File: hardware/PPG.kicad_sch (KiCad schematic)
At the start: 2 parts, among them IC2 MAX86141ENP+T, IC3 SFH_7074

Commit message: Added display block (barely) and freaked out about PPG stuff
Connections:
- net PPG_SCK: now reaches IC2.A2 (SCLK)
- net PPG_MISO: now reaches IC2.A3 (SDO)
- net PPG_MOSI: now reaches IC2.A4 (SDI)
- net PPG_CS: now reaches IC2.A5 (CSB)
- net GND: now reaches IC2.C2 (VDD_DIG)
- net GND: now also IC2.C3 (GND_DIG), IC2.C4 (GND_ANA), IC2.C5 (PD_GND), IC2.D3 (PGND)
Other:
- note added: "MAX86141 requires 1p8 power supply for both core and IO This would require a level translator to communicate with the STM32 Explore * AFE4404 * AFE4490 * OSRAM AS7058 What is my dynamic range requirement? What are my wavelengths? What does my optical stack look like? Can't choose an AFE until the above is settled ^^"

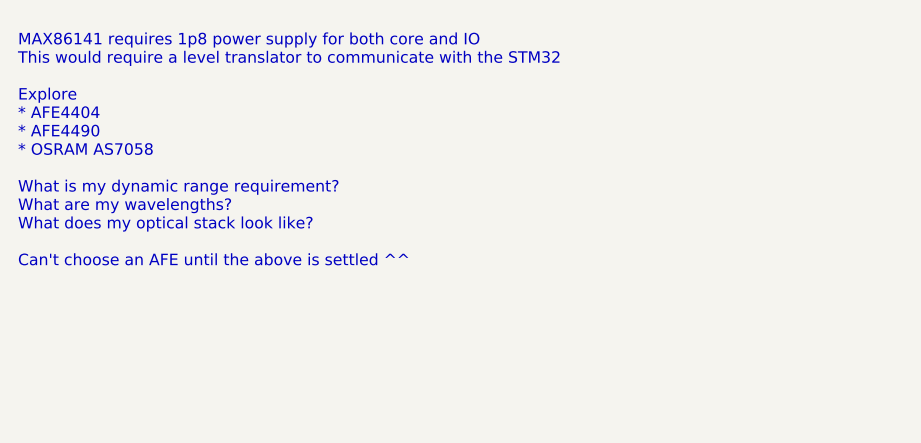
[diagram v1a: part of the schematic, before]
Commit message: Added bluetooth module schematic and environmental perception block"
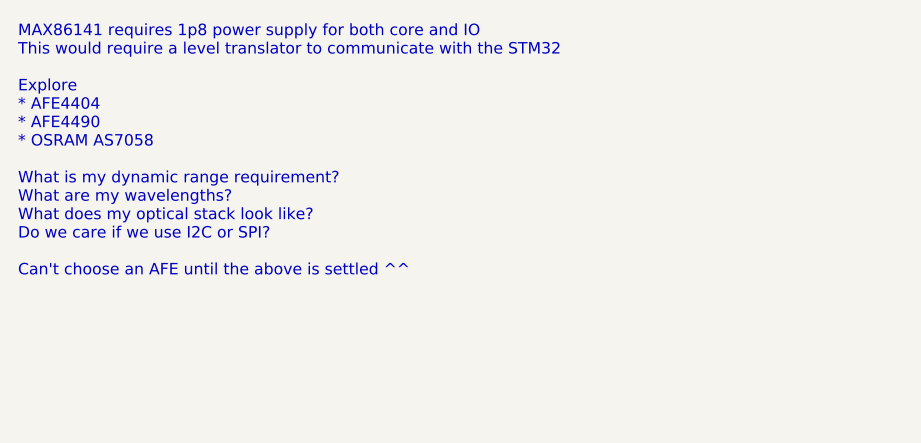
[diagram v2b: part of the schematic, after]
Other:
- note added: "MAX86141 requires 1p8 power supply for both core and IO This would require a level translator to communicate with the STM32 Explore * AFE4404 * AFE4490 * OSRAM AS7058 What is my dynamic range requirement? What are my wavelengths? What does my optical stack look like? Do we care if we use I2C or SPI? Can't choose an AFE until the above is settled ^^"
- note removed: "MAX86141 requires 1p8 power supply for both core and IO This would require a level translator to communicate with the STM32 Explore * AFE4404 * AFE4490 * OSRAM AS7058 What is my dynamic range requirement? What are my wavelengths? What does my optical stack look like? Can't choose an AFE until the above is settled ^^"
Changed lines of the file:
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@@
 	(generator_version "10.0")
 	(paper "A4")
-	(text "MAX86141 requires 1p8 power supply for both core and IO\nThis would require a level translator to communicate with the STM32\n\nExplore\n* AFE4404\n* AFE4490\n* OSRAM AS7058\n\nWhat is my dynamic range requirement?\nWhat are my wavelengths?\nWhat does my optical stack look like?\n\nCan't choose an AFE until the above is settled ^^"
+	(text "MAX86141 requires 1p8 power supply for both core and IO\nThis would require a level translator to communicate with the STM32\n\nExplore\n* AFE4404\n* AFE4490\n* OSRAM AS7058\n\nWhat is my dynamic range requirement?\nWhat are my wavelengths?\nWhat does my optical stack look like?\nDo we care if we use I2C or SPI?\n\nCan't choose an AFE until the above is settled ^^"
 		(exclude_from_sim no)
 		(at 24.892 36.576 0)

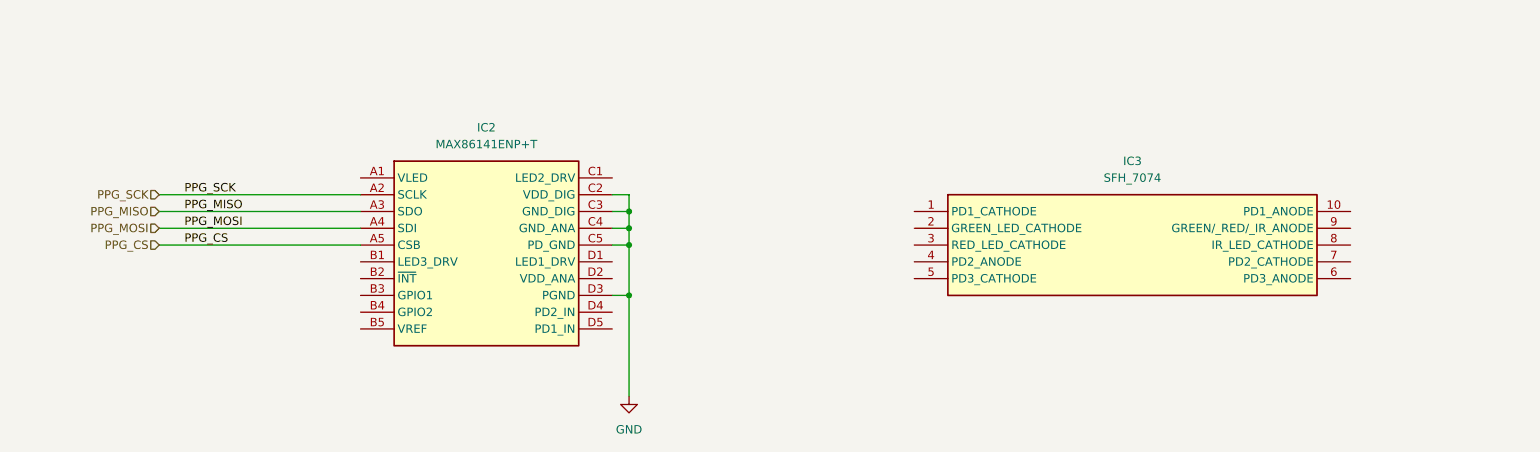
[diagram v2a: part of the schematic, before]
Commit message: Changing barometer, STM32 and power rails
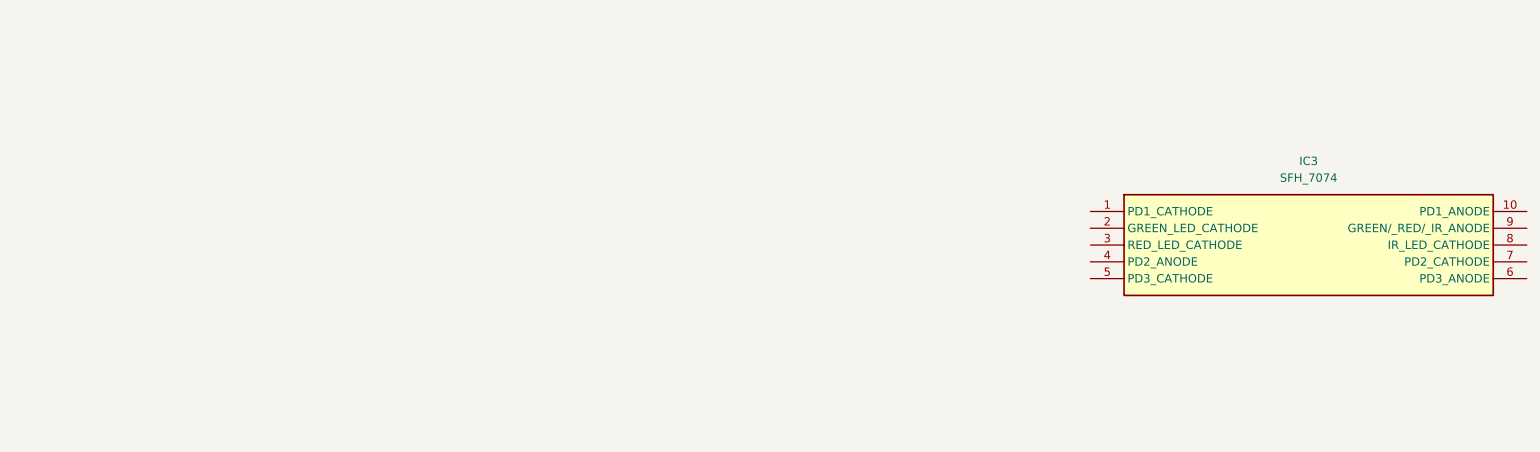
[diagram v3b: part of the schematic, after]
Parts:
- removed IC2: MAX86141ENP+T, BGA20C40P5X4_205X185X50, symbol MAX86141ENP+T:MAX86141ENP+T
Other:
- moved on the sheet: IC3

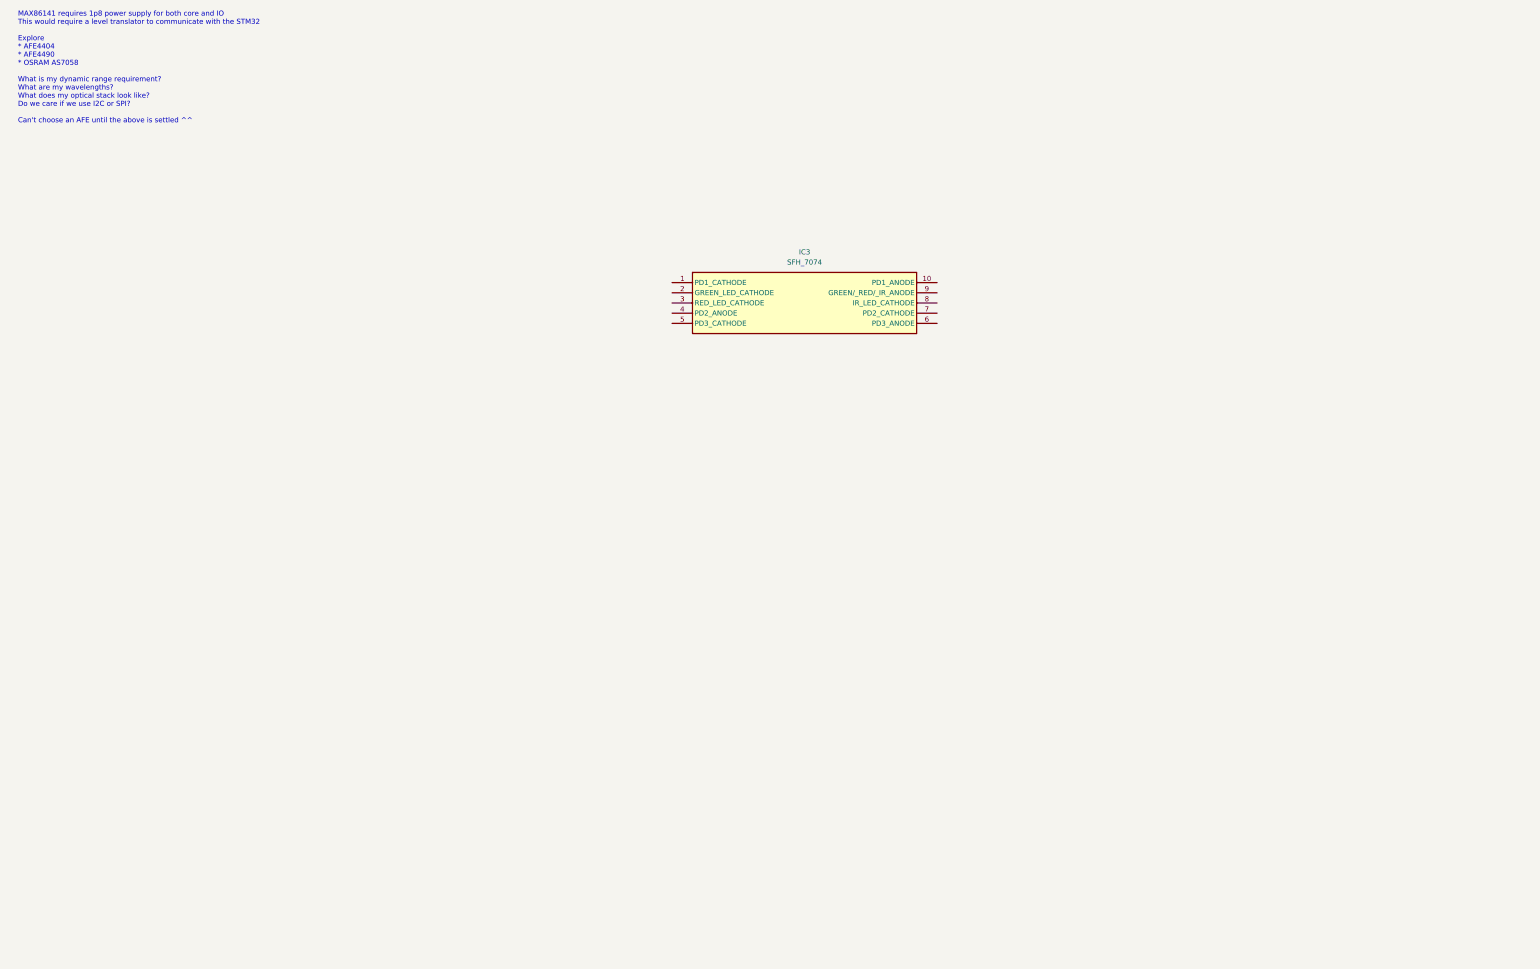
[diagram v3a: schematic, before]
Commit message: Updated schematic to add AFE4403
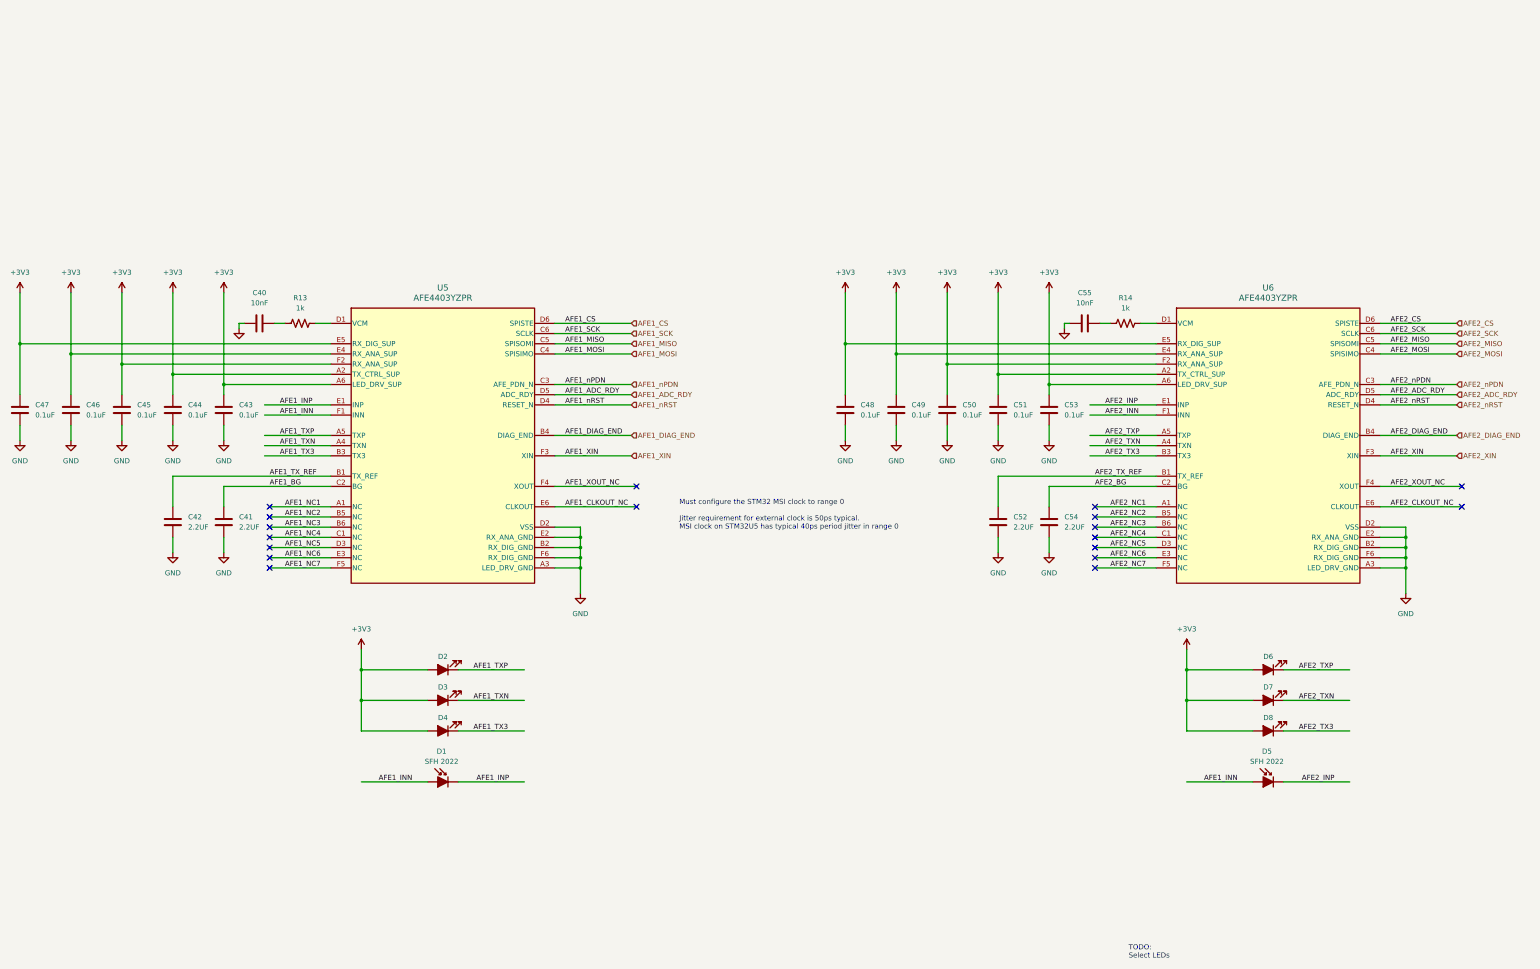
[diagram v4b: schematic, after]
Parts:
- removed IC3: SFH_7074, SFH7074, symbol SFH_7074:SFH_7074
- added C40, C55: 10nF, symbol Device:C
- added C41, C42, C52, C54: 2.2UF, symbol Device:C
- added C43, C44, C45, C46, C47, C48, C49, C50, C51, C53: 0.1uF, symbol Device:C
- added D1, D5: SFH 2022, symbol Device:D_Photo_Filled
- added D2, D3, D4, D6, D7, D8: LED_Filled, symbol Device:LED_Filled
- added R13, R14: 1k, symbol Device:R_US
- added U5, U6: AFE4403YZPR, YZP0036AKAK, symbol AFE4403YZPR:AFE4403YZPR
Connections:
- new net: R14.2, U6.D1 (VCM)
- new net: C40.2, R13.1
- new net: C55.2, R14.1
- new net: R13.2, U5.D1 (VCM)
- new net +3V3: C43.1, C44.1, C45.1, C46.1, C47.1, C48.1, C49.1, C50.1, C51.1, C53.1, D2.2 (A), D3.2 (A), D4.2 (A), D6.2 (A), D7.2 (A), D8.2 (A), U5.A2 (TX_CTRL_SUP), U5.A6 (LED_DRV_SUP), U5.E4 (RX_ANA_SUP), U5.E5 (RX_DIG_SUP), U5.F2 (RX_ANA_SUP), U6.A2 (TX_CTRL_SUP), U6.A6 (LED_DRV_SUP), U6.E4 (RX_ANA_SUP), U6.E5 (RX_DIG_SUP), U6.F2 (RX_ANA_SUP)
- new net AFE1_ADC_RDY: U5.D5 (ADC_RDY)
- new net AFE1_BG: C41.1, U5.C2 (BG)
- new net AFE1_CLKOUT_NC: U5.E6 (CLKOUT)
- new net AFE1_CS: U5.D6 (SPISTE)
- new net AFE1_DIAG_END: U5.B4 (DIAG_END)
- new net AFE1_INN: D1.2 (A), D5.2 (A), U5.F1 (INN)
- new net AFE1_INP: D1.1 (K), U5.E1 (INP)
- new net AFE1_MISO: U5.C5 (SPISOMI)
- new net AFE1_MOSI: U5.C4 (SPISIMO)
- new net AFE1_NC1: U5.A1 (NC)
- new net AFE1_NC2: U5.B5 (NC)
- new net AFE1_NC3: U5.B6 (NC)
- new net AFE1_NC4: U5.C1 (NC)
- new net AFE1_NC5: U5.D3 (NC)
- new net AFE1_NC6: U5.E3 (NC)
- new net AFE1_NC7: U5.F5 (NC)
- new net AFE1_SCK: U5.C6 (SCLK)
- new net AFE1_TX3: D4.1 (K), U5.B3 (TX3)
- new net AFE1_TXN: D3.1 (K), U5.A4 (TXN)
- new net AFE1_TXP: D2.1 (K), U5.A5 (TXP)
- new net AFE1_TX_REF: C42.1, U5.B1 (TX_REF)
- new net AFE1_XIN: U5.F3 (XIN)
- new net AFE1_XOUT_NC: U5.F4 (XOUT)
- new net AFE1_nPDN: U5.C3 (AFE_PDN_N)
- new net AFE1_nRST: U5.D4 (RESET_N)
- new net AFE2_ADC_RDY: U6.D5 (ADC_RDY)
- new net AFE2_BG: C54.1, U6.C2 (BG)
- new net AFE2_CLKOUT_NC: U6.E6 (CLKOUT)
- new net AFE2_CS: U6.D6 (SPISTE)
- new net AFE2_DIAG_END: U6.B4 (DIAG_END)
- new net AFE2_INN: U6.F1 (INN)
- new net AFE2_INP: D5.1 (K), U6.E1 (INP)
- new net AFE2_MISO: U6.C5 (SPISOMI)
- new net AFE2_MOSI: U6.C4 (SPISIMO)
- new net AFE2_NC1: U6.A1 (NC)
- new net AFE2_NC2: U6.B5 (NC)
- new net AFE2_NC3: U6.B6 (NC)
- new net AFE2_NC4: U6.C1 (NC)
- new net AFE2_NC5: U6.D3 (NC)
- new net AFE2_NC6: U6.E3 (NC)
- new net AFE2_NC7: U6.F5 (NC)
- new net AFE2_SCK: U6.C6 (SCLK)
- new net AFE2_TX3: D8.1 (K), U6.B3 (TX3)
- new net AFE2_TXN: D7.1 (K), U6.A4 (TXN)
- new net AFE2_TXP: D6.1 (K), U6.A5 (TXP)
- new net AFE2_TX_REF: C52.1, U6.B1 (TX_REF)
- new net AFE2_XIN: U6.F3 (XIN)
- new net AFE2_XOUT_NC: U6.F4 (XOUT)
- new net AFE2_nPDN: U6.C3 (AFE_PDN_N)
- new net AFE2_nRST: U6.D4 (RESET_N)
- new net GND: C40.1, C41.2, C42.2, C43.2, C44.2, C45.2, C46.2, C47.2, C48.2, C49.2, C50.2, C51.2, C52.2, C53.2, C54.2, C55.1, U5.A3 (LED_DRV_GND), U5.B2 (RX_DIG_GND), U5.D2 (VSS), U5.E2 (RX_ANA_GND), U5.F6 (RX_DIG_GND), U6.A3 (LED_DRV_GND), U6.B2 (RX_DIG_GND), U6.D2 (VSS), U6.E2 (RX_ANA_GND), U6.F6 (RX_DIG_GND)
- no-connect marks 0 -> 18
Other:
- note added: "Must configure the STM32 MSI clock to range 0 Jitter requirement for external clock is 50ps typical. MSI clock on STM32U5 has typical 40ps period jitter in range 0"
- note added: "TODO: Select LEDs"
- note removed: "MAX86141 requires 1p8 power supply for both core and IO This would require a level translator to communicate with the STM32 Explore * AFE4404 * AFE4490 * OSRAM AS7058 What is my dynamic range requirement? What are my wavelengths? What does my optical stack look like? Do we care if we use I2C or SPI? Can't choose an AFE until the above is settled ^^"

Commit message: Updated to the AS5078
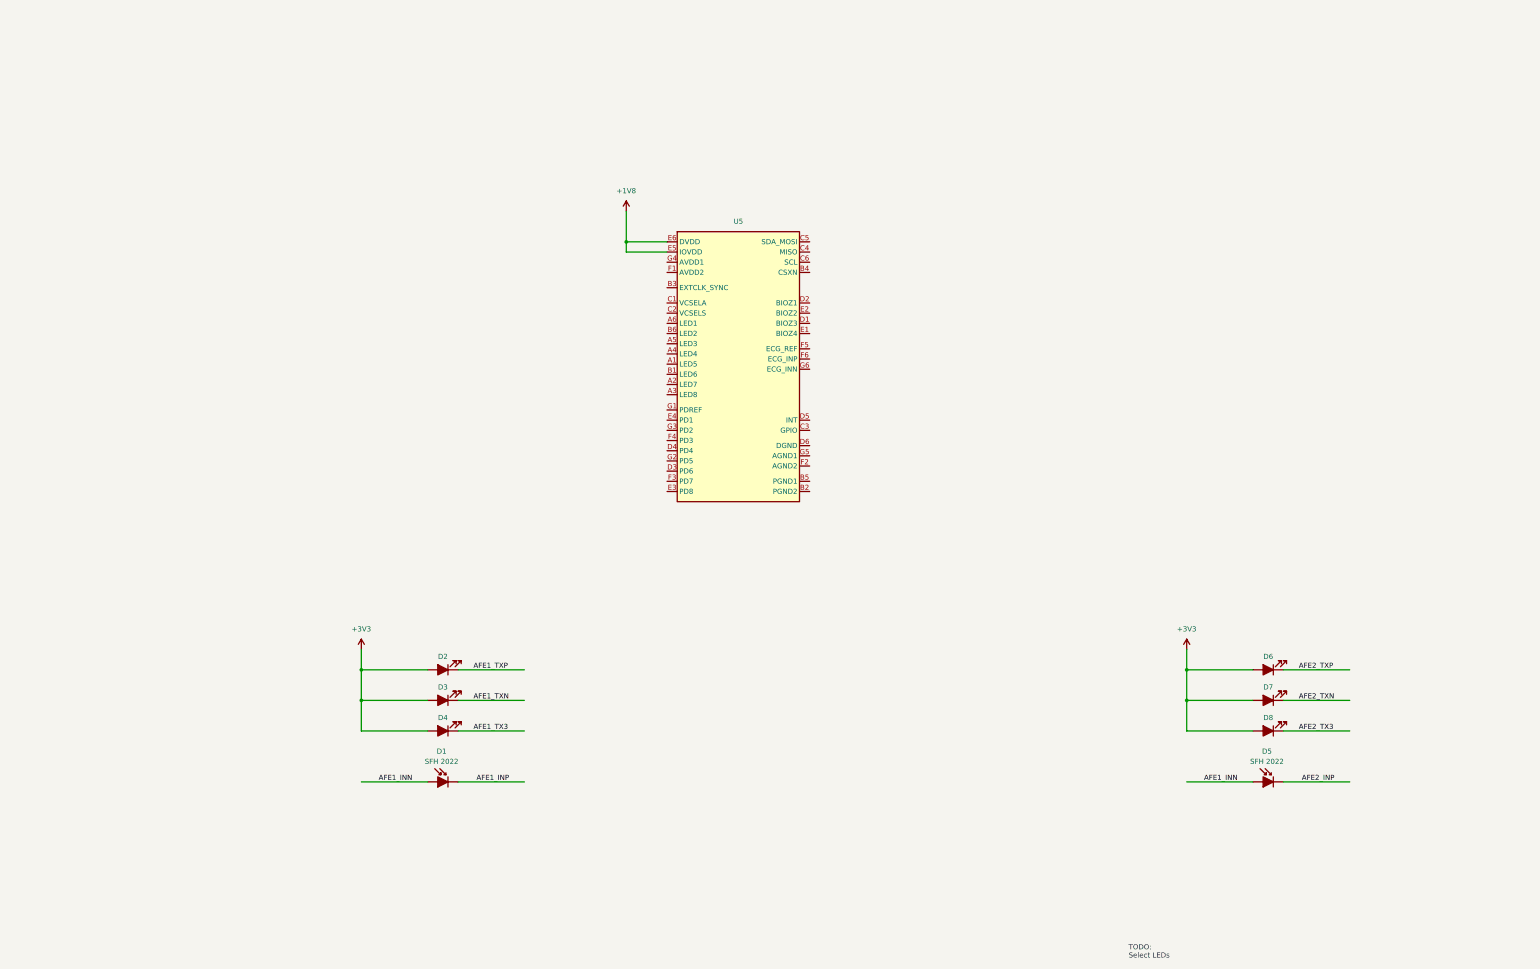
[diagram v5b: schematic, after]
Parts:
- removed C40, C55: 10nF, symbol Device:C
- removed C41, C42, C52, C54: 2.2UF, symbol Device:C
- removed C43, C44, C45, C46, C47, C48, C49, C50, C51, C53: 0.1uF, symbol Device:C
- removed R13, R14: 1k, symbol Device:R_US
- removed U5, U6: AFE4403YZPR, YZP0036AKAK, symbol AFE4403YZPR:AFE4403YZPR
- added U5: (no value), symbol Analog_ADC:AS7058
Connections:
- new net +1V8: U5.E5 (IOVDD), U5.E6 (DVDD)
- no-connect marks 18 -> 0
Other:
- note removed: "Must configure the STM32 MSI clock to range 0 Jitter requirement for external clock is 50ps typical. MSI clock on STM32U5 has typical 40ps period jitter in range 0"
